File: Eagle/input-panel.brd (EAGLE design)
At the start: 40 x 96 mm, 23 parts, among them J1 UJC-HP-3-SMT-TR

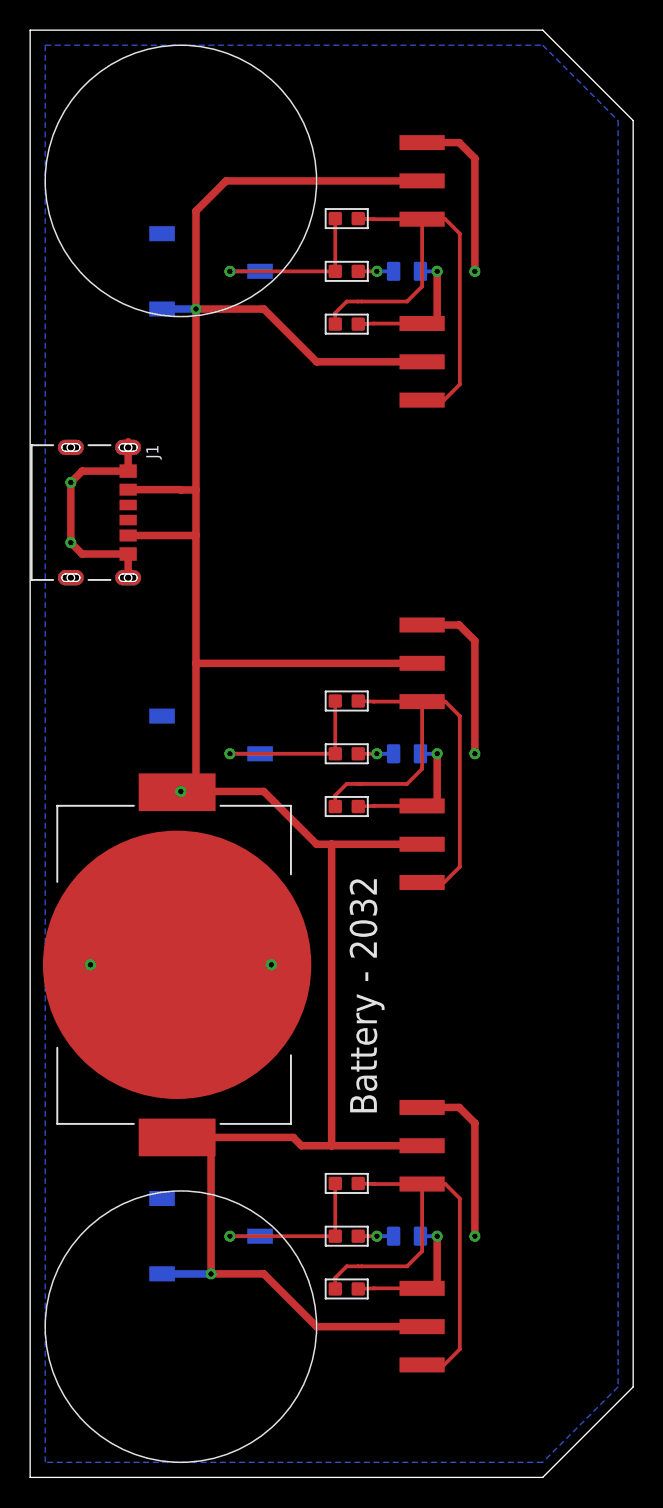
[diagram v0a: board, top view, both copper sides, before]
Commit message: updated input panel
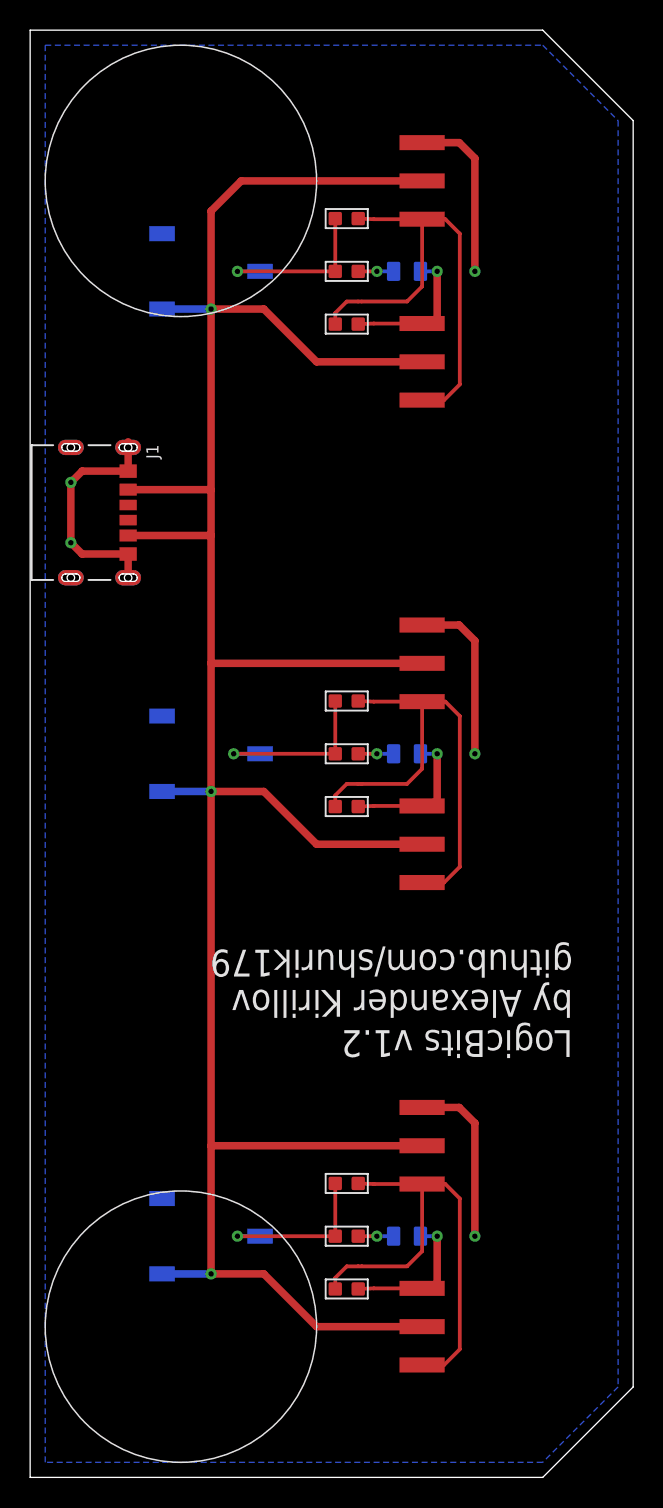
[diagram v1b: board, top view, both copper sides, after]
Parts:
- removed BT1: BAT-HLD-001, BAT-HLD-001:BAT_BAT-HLD-001
- R3, R5, R7: value 1K -> 560
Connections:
- net GND: no longer BT1.N1
- net VCC: no longer BT1.P1, BT1.P2
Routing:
- net GND: track 84.3 -> 78.0 mm, vias 10 -> 8
- net VCC: track 183.0 -> 180.4 mm
- net N$3: track 12.5 -> 11.5 mm
- net N$1: track 12.5 -> 11.5 mm
- net N$2: track 12.5 -> 12.0 mm
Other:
- board text added: "LogicBits v1.2 by Alexander Kirillov github.com/shurik179"
- board text removed: "Battery - 2032"

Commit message: updated for v1.3
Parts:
- removed C4: 1uF, RoverWing-V1.5:0603
- removed R7: 560, RoverWing-V1.5:0603
- removed R8: 220, RoverWing-V1.5:0603
- added C1: 1uF, RoverWing-V1.5:0603
- added R1: 560, RoverWing-V1.5:0603
- added R2: 220, RoverWing-V1.5:0603
- JP3, JP4, JP5, JP6, JP7, JP8: device logicBlocks-AND-v12:SPARKFUN-CONNECTORS_1X03_SMD_RA_MALE -> logicBlocks-AND-v12:SPARKFUN_1X03-SMD-MALE
- moved C2 32.0 mm to (21.0, 44.5)
- moved C3 32.0 mm to (21.0, 76.5)
- moved R3 32.0 mm to (21.0, 48.0)
- moved R4 32.0 mm to (21.0, 51.5)
- moved R5 32.0 mm to (21.0, 80.0)
- moved R6 32.0 mm to (21.0, 83.5)
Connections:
- net GND: now also C1.1; no longer C4.1
- net N$1: now also R1.2, R2.2; no longer R3.2, R4.2
- net N$2: now also R3.2, R4.2; no longer R5.2, R6.2
- net N$3: now also R5.2, R6.2; no longer R7.2, R8.2
- net N$4: now also R3.1; no longer R5.1
- net N$5: now also R1.1; no longer R3.1
- net N$6: now also R5.1; no longer R7.1
- net SIGNAL1: now also C1.2, R2.1; no longer C2.2, R4.1
- net SIGNAL2: now also C2.2, R4.1; no longer C3.2, R6.1
- net SIGNAL3: now also C3.2, R6.1; no longer C4.2, R8.1
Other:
- board text added: "JLCJLCJLCJLC"
- board text added: "LogicBits v1.3 by Alexander Kirillov github.com/shurik179"
- board text removed: "LogicBits v1.2 by Alexander Kirillov github.com/shurik179"
